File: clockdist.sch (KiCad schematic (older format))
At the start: 16 parts, among them U33 74LS258

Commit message: Work in progress
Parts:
- C33: footprint (none) -> Raemixx500:C_Axial_L6.3mm_D2.5mm_P10.16mm
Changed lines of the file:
@@
 F 0 "C33" H 10305 3916 50  0000 L CNN
 F 1 "10n" H 10305 3825 50  0000 L CNN
-F 2 "" H 10228 3720 50  0001 C CNN
+F 2 "Raemixx500:C_Axial_L6.3mm_D2.5mm_P10.16mm" H 10228 3720 50  0001 C CNN
 F 3 "~" H 10190 3870 50  0001 C CNN
 	1    10190 3870

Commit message: Almost all components positioned
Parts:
- E104, E105: footprint (none) -> Raemixx500:EMI_Filter_Long
- E109, E791, E792, E793, E794: footprint (none) -> Raemixx500:C_Axial_L6.3mm_D2.5mm_P10.16mm
- E407: footprint (none) -> Raemixx500:EMI_Filter_Short
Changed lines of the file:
@@
 F 0 "E105" V 5140 3950 50  0000 C CNN
 F 1 "68" V 5240 3950 50  0000 C CNN
-F 2 "" V 5170 3950 50  0001 C CNN
+F 2 "Raemixx500:EMI_Filter_Long" V 5170 3950 50  0001 C CNN
 F 3 "~" H 5240 3950 50  0001 C CNN
 	1    5240 3950
@@
 F 0 "E104" V 5140 4350 50  0000 C CNN
 F 1 "68" V 5240 4350 50  0000 C CNN
-F 2 "" V 5170 4350 50  0001 C CNN
+F 2 "Raemixx500:EMI_Filter_Long" V 5170 4350 50  0001 C CNN
 F 3 "~" H 5240 4350 50  0001 C CNN
 	1    5240 4350
@@
 F 0 "E407" V 9644 3049 50  0000 L CNN
 F 1 "10n" V 9735 3049 50  0000 L CNN
-F 2 "" V 9690 2870 50  0001 C CNN
+F 2 "Raemixx500:EMI_Filter_Short" V 9690 2870 50  0001 C CNN
 F 3 "http://www.murata.com/~/media/webrenewal/support/library/catalog/products/emc/emifil/c31e.ashx?la=en-gb" V 9690 2870 50  0001 C CNN
 	1    9690 2870
@@
 F 0 "E793" H 6225 4816 50  0000 L CNN
 F 1 "47p" H 6225 4725 50  0000 L CNN
-F 2 "" H 6148 4620 50  0001 C CNN
+F 2 "Raemixx500:C_Axial_L6.3mm_D2.5mm_P10.16mm" H 6148 4620 50  0001 C CNN
 F 3 "~" H 6110 4770 50  0001 C CNN
 	1    6110 4770
@@
 F 0 "E792" H 6665 4826 50  0000 L CNN
 F 1 "47p" H 6665 4735 50  0000 L CNN
-F 2 "" H 6588 4630 50  0001 C CNN
+F 2 "Raemixx500:C_Axial_L6.3mm_D2.5mm_P10.16mm" H 6588 4630 50  0001 C CNN
 F 3 "~" H 6550 4780 50  0001 C CNN
 	1    6550 4780
@@
 F 0 "E791" H 7105 4826 50  0000 L CNN
 F 1 "47p" H 7105 4735 50  0000 L CNN
-F 2 "" H 7028 4630 50  0001 C CNN
+F 2 "Raemixx500:C_Axial_L6.3mm_D2.5mm_P10.16mm" H 7028 4630 50  0001 C CNN
 F 3 "~" H 6990 4780 50  0001 C CNN
 	1    6990 4780
@@
 F 0 "E109" H 7545 4836 50  0000 L CNN
 F 1 "47p" H 7545 4745 50  0000 L CNN
-F 2 "" H 7468 4640 50  0001 C CNN
+F 2 "Raemixx500:C_Axial_L6.3mm_D2.5mm_P10.16mm" H 7468 4640 50  0001 C CNN
 F 3 "~" H 7430 4790 50  0001 C CNN
 	1    7430 4790
@@
 F 0 "E794" H 2555 6836 50  0000 L CNN
 F 1 "47p" H 2555 6745 50  0000 L CNN
-F 2 "" H 2478 6640 50  0001 C CNN
+F 2 "Raemixx500:C_Axial_L6.3mm_D2.5mm_P10.16mm" H 2478 6640 50  0001 C CNN
 F 3 "~" H 2440 6790 50  0001 C CNN
 	1    2440 6790

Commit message: Work in progress
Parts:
- removed E104, E105: 68, Raemixx500:EMI_Filter_Long, symbol Device:R
- added E104, E105: 68, Raemixx500:EMI_Filter_Long, symbol emi_filter_lcl_small:EMI_Filter_LCL
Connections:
- net GND: now also E104.2, E105.2
- net ~CCKQ_A: now also E105.3
- net ~CCK_A: now also E104.3
- net at RP103.5 (R3.1), U33.7: now also E104.1
- net at RP103.7 (R4.1), U33.9: now also E105.1

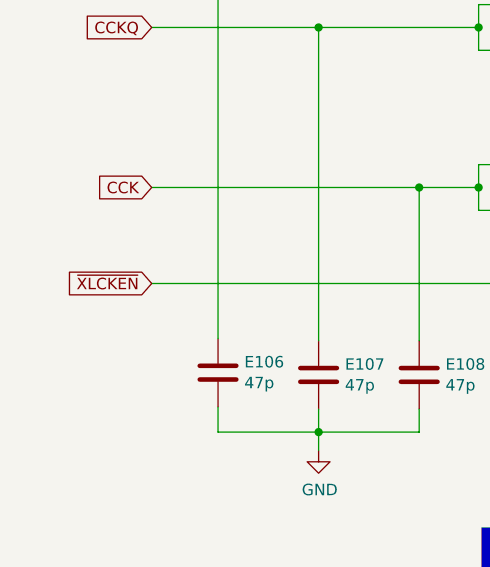
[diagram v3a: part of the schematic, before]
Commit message: Fix a lot of ERC/DRC errors
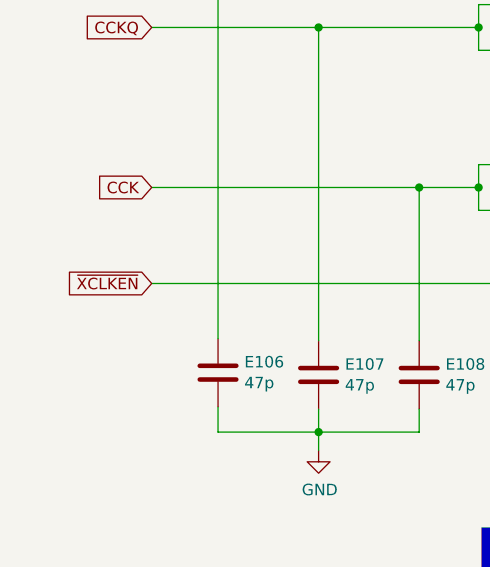
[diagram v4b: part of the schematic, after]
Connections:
- net ~XLCKEN renamed ~XCLKEN
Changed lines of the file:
@@
 EESchema Schematic File Version 4
-LIBS:Raemix500-cache
-EELAYER 29 0
+EELAYER 30 0
 EELAYER END
 $Descr A4 11693 8268
@@
 	4090 4370 1710 4370
 Text GLabel 1710 4370 0    50   Input ~ 0
-~XLCKEN
+~XCLKEN
 Wire Wire Line
 	3640 3450 3640 3550
